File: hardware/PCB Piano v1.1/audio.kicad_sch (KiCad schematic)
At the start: 30 parts, among them J3 AudioJack4_SwitchTR1R2S, J8 Conn_01x02_Pin, SW2 RotaryEncoder, U11 TVL320DAC3100

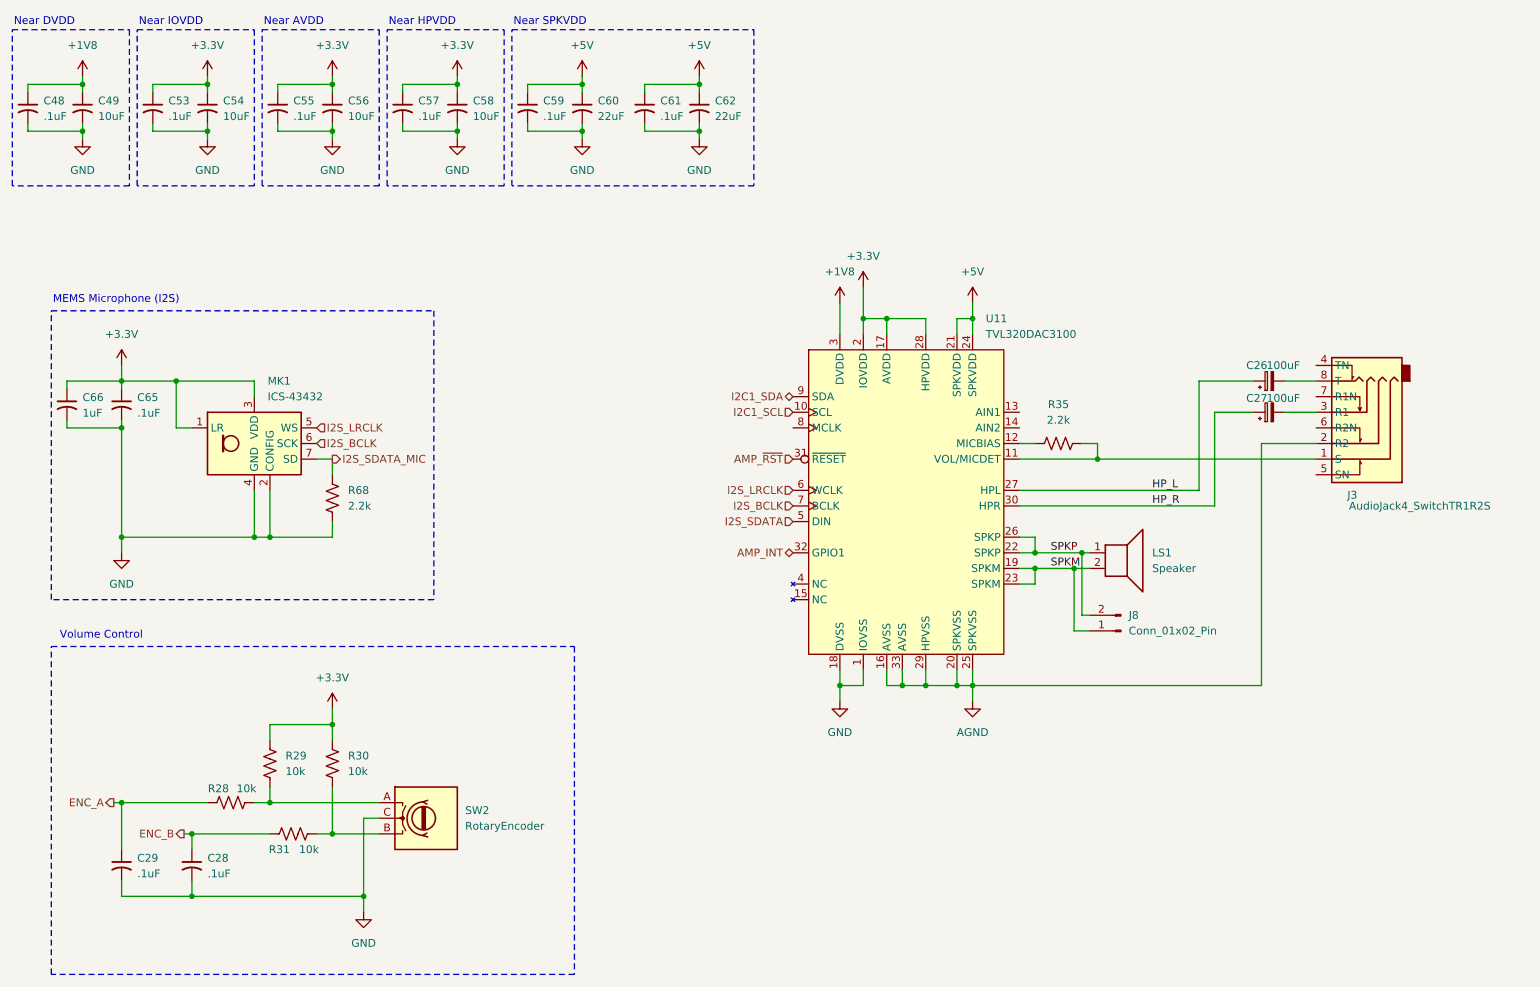
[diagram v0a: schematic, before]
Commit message: Development Phase - PCB Complete - ERC/DRC in progress
Development commit. PBC layout complete. ERC/DRC checks in progress. Swapped some connectors for JST connectors with Adafruit-style polarization.
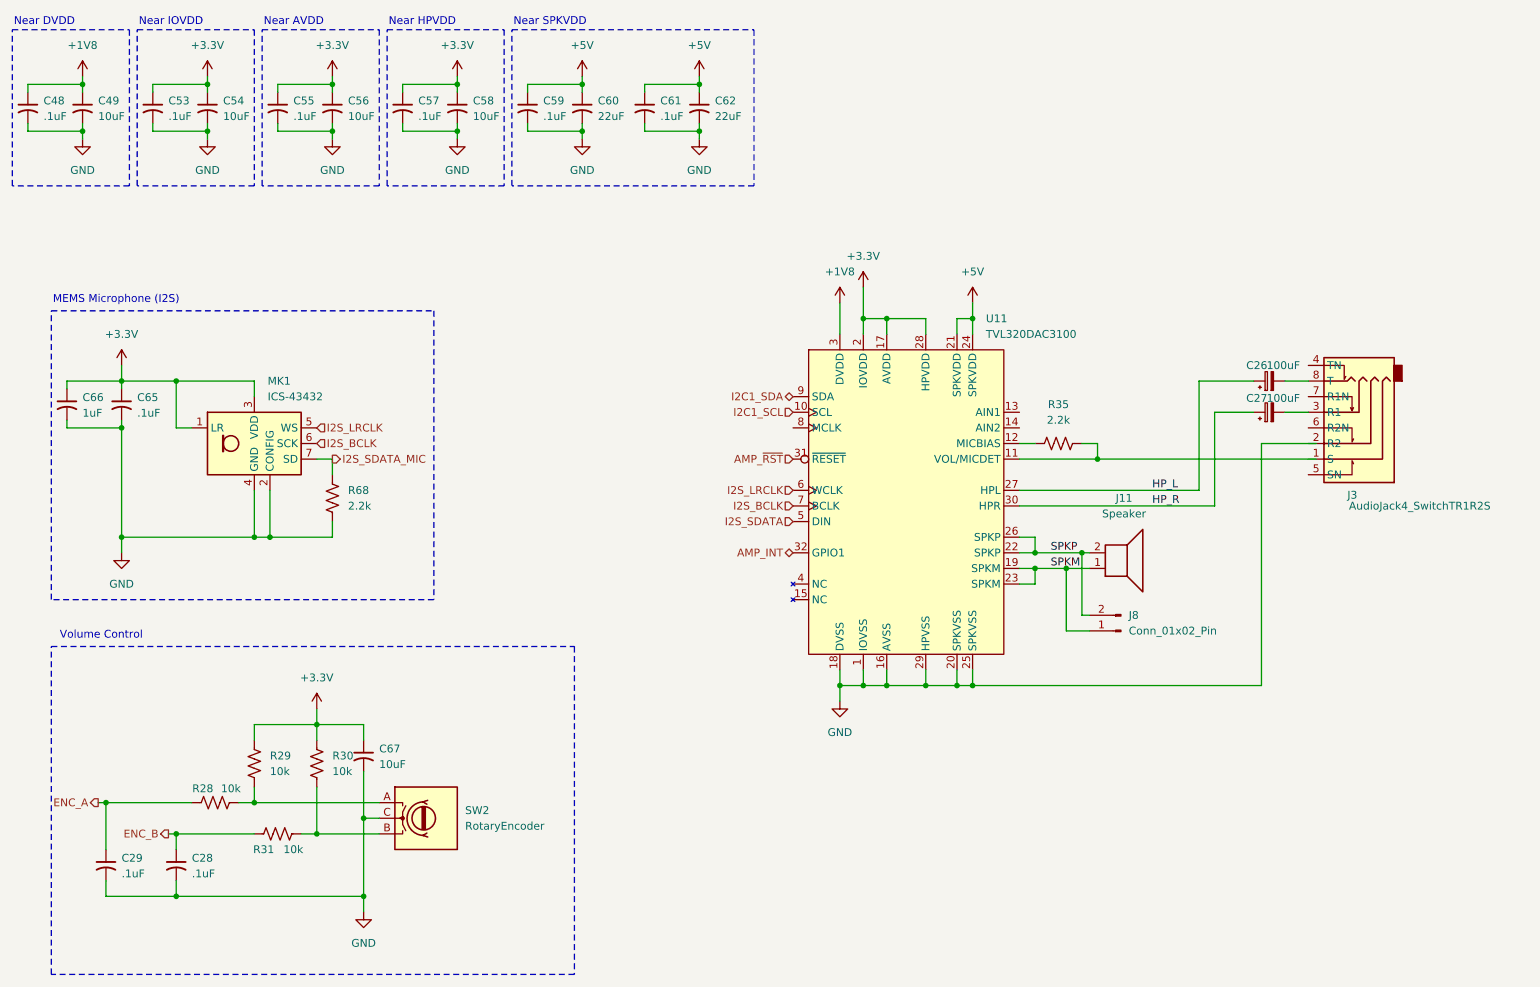
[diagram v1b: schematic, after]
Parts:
- added C67: 10uF, Capacitor_SMD:C_0603_1608Metric, symbol Device:C_Small_US
- J11: renamed from LS1; footprint PCBPiano_Footprints:TestPoint_2Pads_2.5mmx2.5mm_5mmSpacing -> Connector_JST:JST_PH_B2B-PH-SM4-TB_1x02-1MP_P2.00mm_Vertical
- J8: footprint Connector_JST:JST_SH_BM03B-SRSS-TB_1x03-1MP_P1.00mm_Vertical -> Connector_PinHeader_2.54mm:PinHeader_1x02_P2.54mm_Vertical_SMD_Pin1Left
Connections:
- net +3.3V: now also C67.1
- net GND: now also U11.16 (AVSS), U11.20 (SPKVSS), U11.25 (SPKVSS), U11.29 (HPVSS), C67.2
- net SPKM: now also J11.1; no longer J11.2
- net SPKP: now also J11.2; no longer J11.1
- net at R35.2, U11.11 (VOL/MICDET): no longer J3.1 (S)
- removed net AGND: J3.2 (R2), U11.16 (AVSS), U11.20 (SPKVSS), U11.25 (SPKVSS), U11.29 (HPVSS), U11.33 (AVSS)
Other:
- moved on the sheet: C28, C29, J3, R28, R29, R30, R31

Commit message: Firmware architecture complete - PCB revision with new charger.
Firmware Architecture Complete

- Added MP2724 charger driver
- Added TLV320DAC3100 driver
- Added MTCH2120 touch driver
- Added PCA9685 driver
- Added DotStar driver
- Added rotary encoder driver
- Added touch and LED maps
- Added control/audio/voice managers
- Added audio command queue
- Added Core1 audio architecture
- Added status LED system
- Added LED animation framework

Changes hardware schematic and PCB to accommodate a newer-style USB-C sink battery charger chip and USB data MUX to protect MCU while powered off.
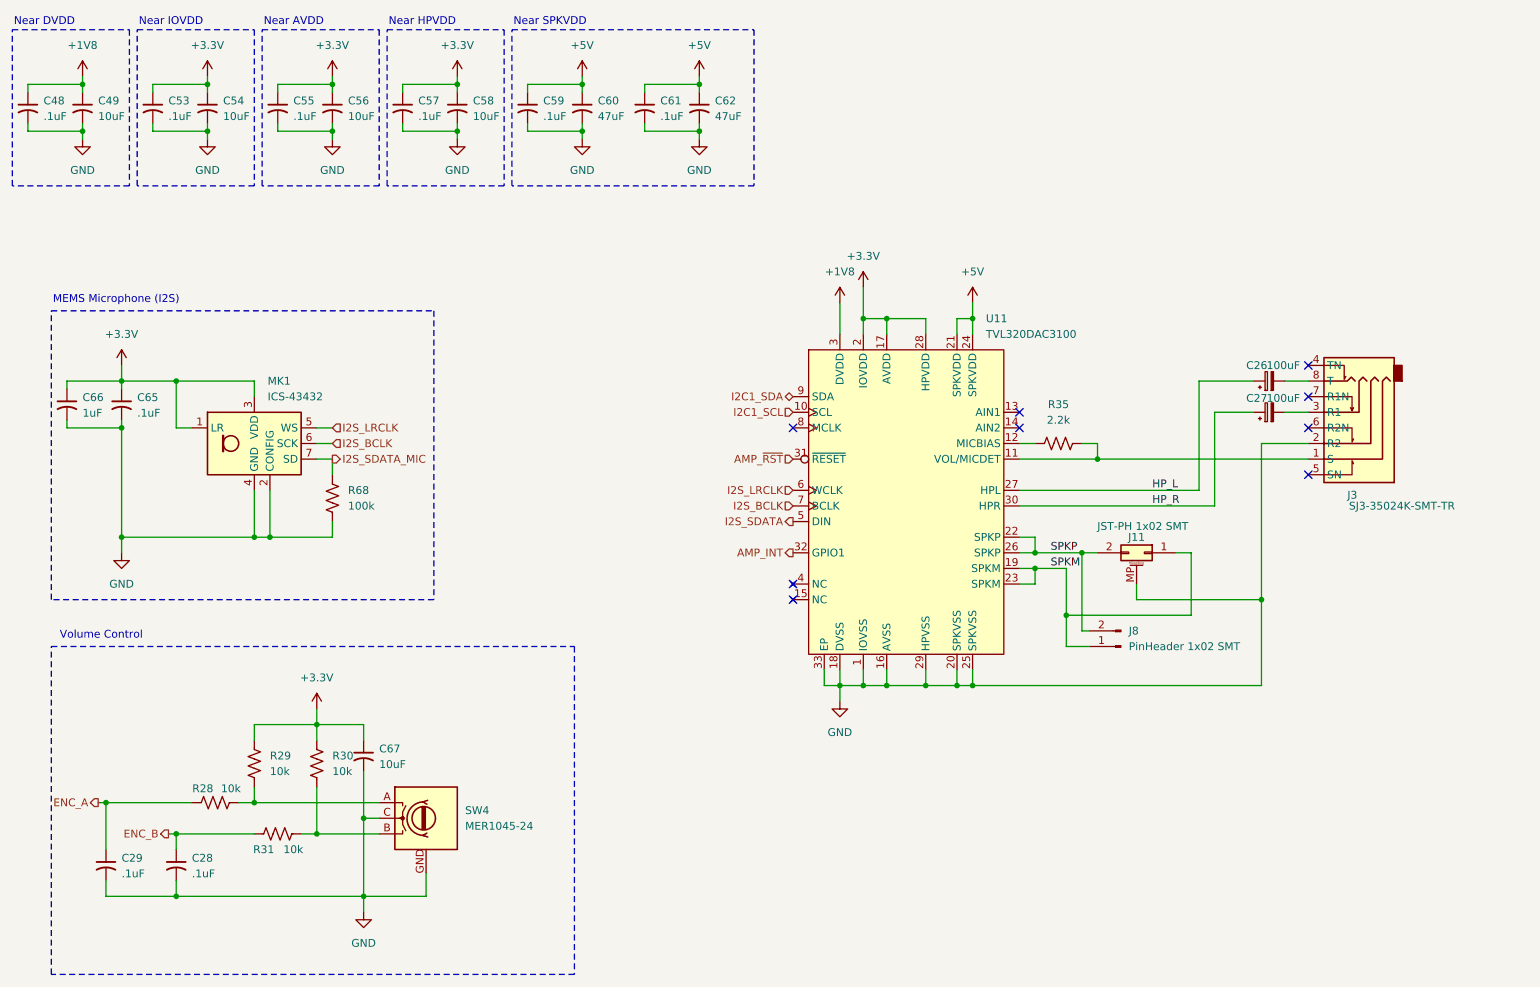
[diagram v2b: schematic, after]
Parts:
- C49, C54, C56, C58, C67: footprint Capacitor_SMD:C_0603_1608Metric -> Capacitor_SMD:C_0805_2012Metric
- C60, C62: value 22uF -> 47uF; footprint Capacitor_Tantalum_SMD:CP_EIA-6032-20_AVX-F -> Capacitor_Tantalum_SMD:CP_EIA-3528-15_AVX-H
- J11: value Speaker -> JST-PH 1x02 SMT; symbol Device:Speaker -> Connector_Generic_MountingPin:Conn_02x01_MountingPin
- J3: value AudioJack4_SwitchTR1R2S -> SJ3-35024K-SMT-TR
- J8: value Conn_01x02_Pin -> PinHeader 1x02 SMT
- R68: value 2.2k -> 100k
- SW4: renamed from SW2; value RotaryEncoder -> MER1045-24; symbol Device:RotaryEncoder -> PCB Piano Symbols:RotaryEncoder_MP
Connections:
- net GND: now also J11.MP (MountPin), J3.2 (R2), SW4.GND (MountPoints), U11.33 (EP)
- net at J3.1 (S): now also R35.2, U11.11 (VOL/MICDET)
- no-connect marks 0 -> 9
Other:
- moved on the sheet: J8

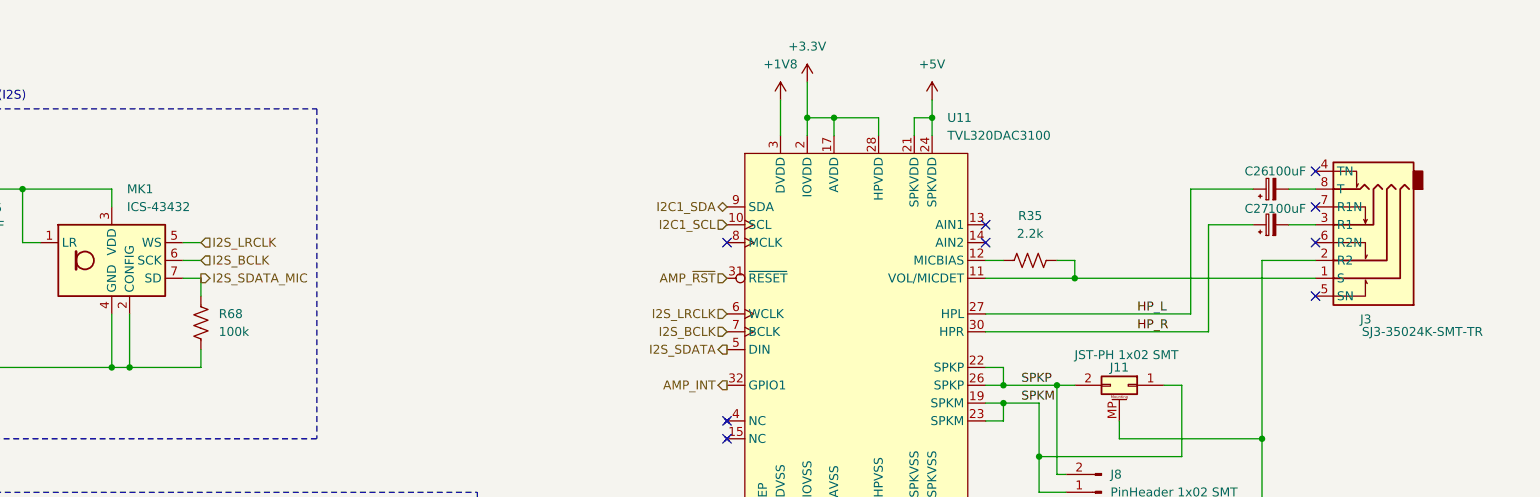
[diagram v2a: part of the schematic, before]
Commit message: PCB Finalized and Ordered. Firmware near completion.
PCB Finalized and Ordered. Final revisions included fixing bugs on some peripheral chips. Also added an RTC circuit after realizing the SD card could benefit from adding file timestamps.

Firmware near completion. Still need to finalize some SD card operations. Synth audio core is finished and all the board peripheral chip drivers were completed.
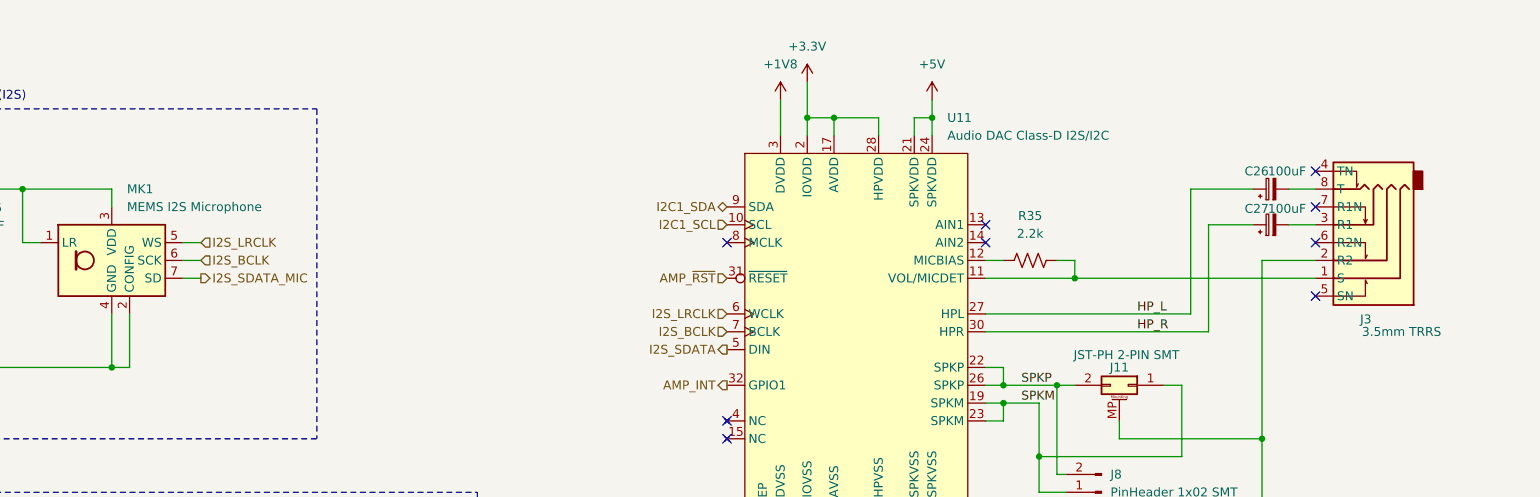
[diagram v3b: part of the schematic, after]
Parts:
- removed R68: 100k, Resistor_SMD:R_0603_1608Metric, symbol Device:R_US
- C26, C27: DigiKey_Part_Number (none) -> 718-2373-1-ND; Manufacturer Part Number (none) -> TMCMA0J107MTRF; Volt Rating (none) -> 10V
- C28, C29, C48, C53, C55, C57, C59, C61, C65: DigiKey_Part_Number (none) -> 1276-1935-2-ND; Manufacturer Part Number (none) -> CL10B104KB8NNWC; Volt Rating (none) -> 10V
- C49, C54, C56, C58, C67: DigiKey_Part_Number (none) -> 490-10516-1-ND; Manufacturer Part Number (none) -> GRM21BR71A106KA73L GRM21BR71A106KA73L GRM21BR71A106KA73L GR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; Volt Rating (none) -> 10V
- C60, C62: DigiKey_Part_Number (none) -> TAJB476K010RNJ; Manufacturer Part Number (none) -> TAJB476K010RNJ; Volt Rating (none) -> 10V
- C66: DigiKey_Part_Number (none) -> 1276-1184-1-ND; Manufacturer Part Number (none) -> CL10B105KA8NNNC; Volt Rating (none) -> 10V
- J11: value JST-PH 1x02 SMT -> JST-PH 2-PIN SMT; DigiKey_Part_Number (none) -> JST-PH 2-PIN SMT; Manufacturer Part Number (none) -> B2B-PH-SM4-TB
- J3: value SJ3-35024K-SMT-TR -> 3.5mm TRRS; DigiKey_Part_Number (none) -> SJ3-35024K-SMT-TR; Manufacturer Part Number (none) -> SJ3-35024K-SMT-TR
- J8: footprint Connector_PinHeader_2.54mm:PinHeader_1x02_P2.54mm_Vertical_SMD_Pin1Left -> Connector_PinHeader_2.54mm:PinHeader_1x02_P2.54mm_Vertical_SMD_Pin1Right
- MK1: value ICS-43432 -> MEMS I2S Microphone; DigiKey_Part_Number (none) -> ICS-43432; Manufacturer Part Number (none) -> ICS-43432
- SW4: DigiKey_Part_Number (none) -> MER1045-24; Manufacturer Part Number (none) -> MER1045-24
- U11: value TVL320DAC3100 -> Audio DAC Class-D I2S/I2C; DigiKey_Part_Number (none) -> TVL320DAC3100; Manufacturer Part Number (none) -> TVL320DAC3100
